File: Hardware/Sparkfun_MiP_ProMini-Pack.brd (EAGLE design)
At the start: 41.4 x 63.8 mm, 47 parts, among them Q1 8MHz, U1 ATMEGA328, U2 MIC5205, U3 TS3USB221A

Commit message: added ProdID's  to parts
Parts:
- C1, C10, C2, C3, C4: device SparkFun:0603-CAP -> SparkFun-Capacitors:0603-CAP
- D3: device Testing:0603-LED-ALT1 -> SparkFun-LED:LED-0603
- R6: device SparkFun:0603-RES -> SparkFun-Resistors:0603-RES
- S1: device Testing:TACTILE-SWITCH-SMD-ALT01 -> SparkFun-Electromechanical:TACTILE-SWITCH-SMD
- U1: device SparkFun:TQFP32-08 -> SparkFun-DigitalIC:TQFP32-08
- U2: device SparkFun:SOT23-5 -> SparkFun-PowerIC:SOT23-5
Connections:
- net GND: no longer S1.2
- net RESET: no longer S1.4
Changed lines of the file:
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@@
 <?xml version="1.0" encoding="utf-8"?>
 <!DOCTYPE eagle SYSTEM "eagle.dtd">
-<eagle version="6.6.0">
+<eagle version="6.5.0">
 <drawing>
 <settings>
@@
 <elements>
 <element name="R2" library="SparkFun" package="0603-RES" value="10K" x="11.3538" y="23.0632" rot="R90"/>
-<element name="C3" library="SparkFun" package="0603-CAP" value="0.1uF" x="18.542" y="41.275" rot="R270"/>
-<element name="C1" library="SparkFun" package="0603-CAP" value="0.1uF" x="21.463" y="40.132"/>
-<element name="R6" library="SparkFun" package="0603-RES" value="330" x="21.463" y="44.958"/>
-<element name="D3" library="Testing" package="0603-LED-ALT1" value="Green" x="21.463" y="46.482" rot="R90"/>
+<element name="C3" library="SparkFun-Capacitors" package="0603-CAP" value="0.1uF" x="18.542" y="41.275" rot="R270">
+<attribute name="PROD_ID" value="CAP-00810" x="18.542" y="41.275" size="1.778" layer="27" rot="R270" display="off"/>
+<attribute name="VALUE" value="0.1uF" x="18.542" y="41.275" size="1.778" layer="27" rot="R270" display="off"/>
+</element>
+<element name="C1" library="SparkFun-Capacitors" package="0603-CAP" value="0.1uF" x="21.463" y="40.132">
+<attribute name="PROD_ID" value="CAP-00810" x="21.463" y="40.132" size="1.778" layer="27" display="off"/>
+<attribute name="VALUE" value="0.1uF" x="21.463" y="40.132" size="1.778" layer="27" display="off"/>
+</element>
+<element name="R6" library="SparkFun-Resistors" package="0603-RES" value="330" x="21.463" y="44.958">
+<attribute name="PROD_ID" value="RES-00818" x="21.463" y="44.958" size="1.778" layer="27" display="off"/>
+<attribute name="VALUE" value="330" x="21.463" y="44.958" size="1.778" layer="27" display="off"/>
+</element>
+<element name="D3" library="SparkFun-LED" package="LED-0603" value="Green" x="21.463" y="46.482" rot="R90">
+<attribute name="PROD_ID" value="DIO-00821" x="21.463" y="46.482" size="1.778" layer="27" rot="R90" display="off"/>
+<attribute name="VALUE" value="GREEN" x="21.463" y="46.482" size="1.778" layer="27" rot="R90" display="off"/>
+</element>
 <element name="JP6" library="SparkFun" package="1X12" value="" x="13.716" y="18.288" smashed="yes" rot="MR90">
 <attribute name="NAME" x="15.5448" y="16.9418" size="1.27" layer="26" ratio="10" rot="MR90"/>
@@
 </element>
 <element name="JP2" library="SparkFun" package="1X02" value="" x="16.637" y="29.591" rot="MR270"/>
-<element name="U1" library="SparkFun" package="TQFP32-08" value="ATMEGA328" x="21.59" y="33.528" rot="R135"/>
+<element name="U1" library="SparkFun-DigitalIC" package="TQFP32-08" value="ATMEGA328" x="21.59" y="33.528" rot="R135">
+<attribute name="PROD_ID" value="IC-09069" x="21.59" y="33.528" size="1.778" layer="27" rot="R135" display="off"/>
+<attribute name="VALUE" value="ATMEGA328P" x="21.59" y="33.528" size="1.778" layer="27" rot="R135" display="off"/>
+</element>
 <element name="JP1" library="SparkFun" package="1X06" value="FTDI Basic" x="14.986" y="4.826"/>
-<element name="C2" library="SparkFun" package="0603-CAP" value="0.1uF" x="16.51" y="23.749" rot="R270"/>
+<element name="C2" library="SparkFun-Capacitors" package="0603-CAP" value="0.1uF" x="16.51" y="23.749" rot="R270">
+<attribute name="PROD_ID" value="CAP-00810" x="16.51" y="23.749" size="1.778" layer="27" rot="R270" display="off"/>
+<attribute name="VALUE" value="0.1uF" x="16.51" y="23.749" size="1.778" layer="27" rot="R270" display="off"/>
+</element>
 <element name="R1" library="SparkFun" package="0603-RES" value="DNP" x="19.558" y="29.591" rot="MR180"/>
 <element name="R3" library="SparkFun" package="0603-RES" value="DNP" x="19.558" y="27.051" rot="MR180"/>
-<element name="S1" library="Testing" package="TACTILE-SWITCH-SMD-ALT01" value="Reset" x="21.336" y="51.054"/>
+<element name="S1" library="SparkFun-Electromechanical" package="TACTILE-SWITCH-SMD" value="Reset" x="21.336" y="51.054">
+<attribute name="PROD_ID" value="SWCH-08247" x="21.336" y="51.054" size="1.778" layer="27" display="off"/>
+</element>
 <element name="JP3" library="SparkFun" package="1X02" value="" x="16.637" y="40.005" rot="MR270"/>
 <element name="Q1" library="SparkFun-FreqCtrl" package="RESONATOR-SMD" value="8MHz" x="25.908" y="27.559" rot="R270">
@@
 <attribute name="PROD_ID" value="RES-07856" x="20.066" y="16.256" size="1.778" layer="27" rot="R180" display="off"/>
 </element>
-<element name="C4" library="SparkFun" package="0603-CAP" value="0.1uF" x="23.495" y="21.59"/>
+<element name="C4" library="SparkFun-Capacitors" package="0603-CAP" value="0.1uF" x="23.495" y="21.59">
+<attribute name="PROD_ID" value="CAP-00810" x="23.495" y="21.59" size="1.778" layer="27" display="off"/>
+<attribute name="VALUE" value="0.1uF" x="23.495" y="21.59" size="1.778" layer="27" display="off"/>
+</element>
 <element name="JP10" library="SparkFun-Connectors" package="1X01" value="M01PTH" x="31.496" y="18.288"/>
 <element name="SJ5" library="SparkFun-Passives" package="PAD-JUMPER-2-NC_BY_TRACE_YES_SILK" value="D2 Jumper" x="31.242" y="21.844" rot="R90"/>
@@
 <element name="SJ1" library="SparkFun-Passives" package="PAD-JUMPER-3-2OF3_NC_BY_PASTE_YES_SILK_FULL_BOX" value="" x="10.922" y="25.908"/>
 <element name="SJ3" library="SparkFun-Passives" package="PAD-JUMPER-3-2OF3_NC_BY_PASTE_YES_SILK_FULL_BOX" value="" x="11.176" y="49.784"/>
-<element name="C10" library="SparkFun" package="0603-CAP" value="0.1uF" x="28.702" y="11.43" rot="R270"/>
+<element name="C10" library="SparkFun-Capacitors" package="0603-CAP" value="0.1uF" x="28.702" y="11.43" rot="R270">
+<attribute name="PROD_ID" value="CAP-00810" x="28.702" y="11.43" size="1.778" layer="27" rot="R270" display="off"/>
+<attribute name="VALUE" value="0.1uF" x="28.702" y="11.43" size="1.778" layer="27" rot="R270" display="off"/>
+</element>
 <element name="C13" library="SparkFun" package="EIA3216" value="10uF" x="26.416" y="11.43" rot="R90"/>
-<element name="U2" library="SparkFun" package="SOT23-5" value="MIC5205" x="22.606" y="11.43" rot="R270"/>
+<element name="U2" library="SparkFun-PowerIC" package="SOT23-5" value="MIC5205" x="22.606" y="11.43" rot="R270">
+<attribute name="PROD_ID" value="VREG-00822" x="22.606" y="11.43" size="1.778" layer="27" rot="R270" display="off"/>
+</element>
 <element name="C19" library="SparkFun" package="EIA3216" value="10uF" x="18.542" y="11.43" rot="R90"/>
 <element name="FID1" library="SparkFun-Aesthetics" package="FIDUCIAL-1X2" value="FIDUCIAL1X2" x="10.16" y="5.08"/>
@@
 </polygon>
 <contactref element="S1" pad="1"/>
-<contactref element="S1" pad="2"/>
 <contactref element="C3" pad="1"/>
 <contactref element="C1" pad="1"/>
@@
 <contactref element="JP6" pad="2"/>
 <contactref element="Q1" pad="2"/>
+<contactref element="U1" pad="21"/>
+<contactref element="U1" pad="3"/>
 <contactref element="U1" pad="5"/>
-<contactref element="U1" pad="3"/>
-<contactref element="U1" pad="21"/>
 <contactref element="JP1" pad="5"/>
 <contactref element="JP1" pad="6"/>
@@
 <contactref element="C2" pad="1"/>
 <contactref element="S1" pad="3"/>
-<contactref element="S1" pad="4"/>
 <wire x1="18.542" y1="49.149" x2="22.225" y2="49.149" width="0.254" layer="1"/>
 <wire x1="22.225" y1="49.149" x2="24.13" y2="49.149" width="0.254" layer="1"/>

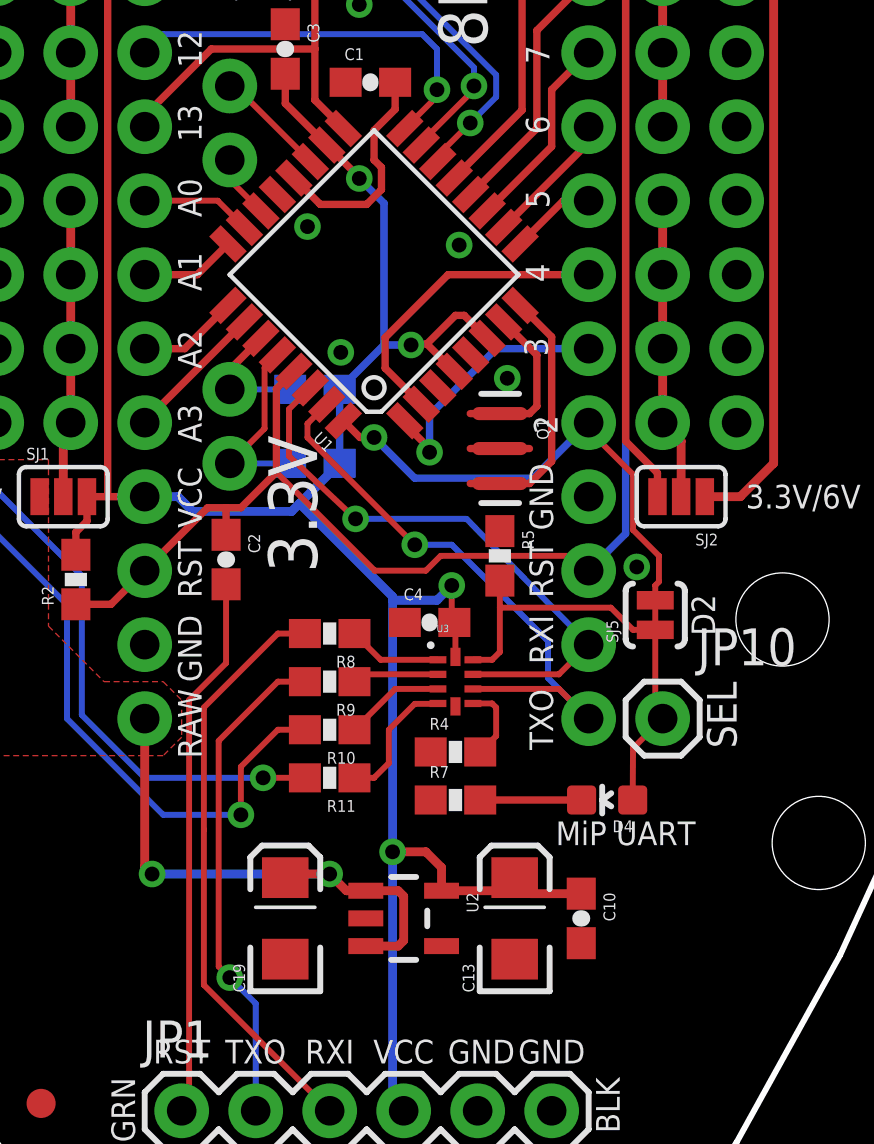
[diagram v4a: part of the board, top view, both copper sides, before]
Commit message: corrected isolate to 12mil made some layout changes to accomidate.
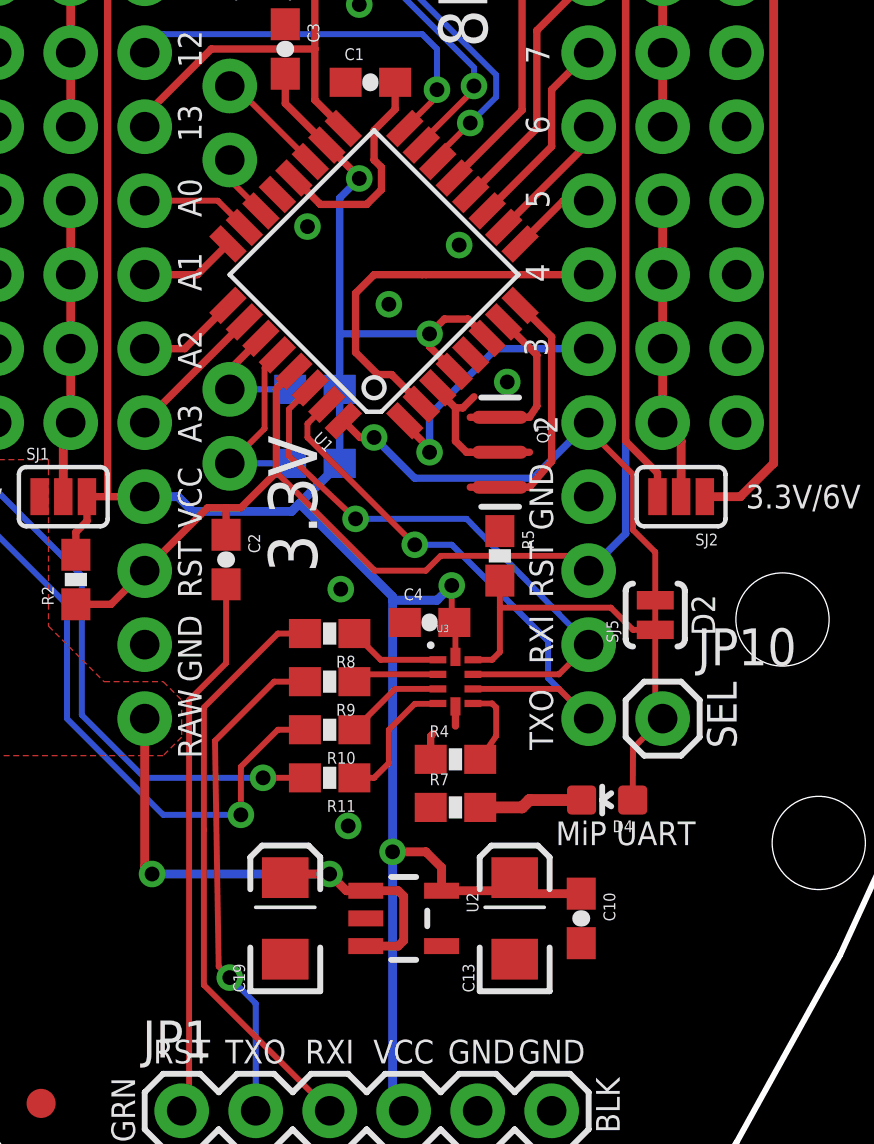
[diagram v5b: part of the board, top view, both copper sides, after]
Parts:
- moved R4 0.25 mm to (24.4, 16.9)
- moved R7 0.25 mm to (24.4, 15.2)
- moved Q1 0.13 mm to (25.9, 27.4)
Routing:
- net GND: track 0.00 -> 5.14 mm, vias 9 -> 10
- net D4: track 10.7 -> 13.3 mm
- net VCC: track 135.7 -> 136.6 mm
